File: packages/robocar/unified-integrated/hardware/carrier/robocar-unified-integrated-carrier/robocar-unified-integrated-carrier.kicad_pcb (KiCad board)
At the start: 2 copper layers, 94 x 100 mm, 108 parts, among them J1 IDC 2x7 head cable, J11 Test: 3V3 5V GND VBAT, J12 Test: GND SDA SCL RST, J13 GND post, J14 GND post, J15 UART0 TX tap, J16 IDC 2x7 head cable, J17 IDC 2x7 head cable, J18 GPIO A/B, J19 Speaker, J2 IDC 2x7 head cable, J20 Pan servo (SG90), J21 Tilt servo (SG90), J22 Left RGB LED, J23 Right RGB LED, J3 XT30 pack in, J5 Motor left, J6 Motor right, J7 RCWL-1601 front, J8 RCWL-1601 rear, J9 SSD1306 0.91in, U1 XIAO ESP32-S3 Sense, U10 TPS563208, U2 AMS1117-3.3, U3 XIAO ESP32-S3 Sense, U4 XIAO ESP32-S3 Sense, U5 TCA9548APWR, U6 PCA9685PW, U7 TB6612FNG, U8 MAX98357AETE+, U9 MCP23017-E/SS

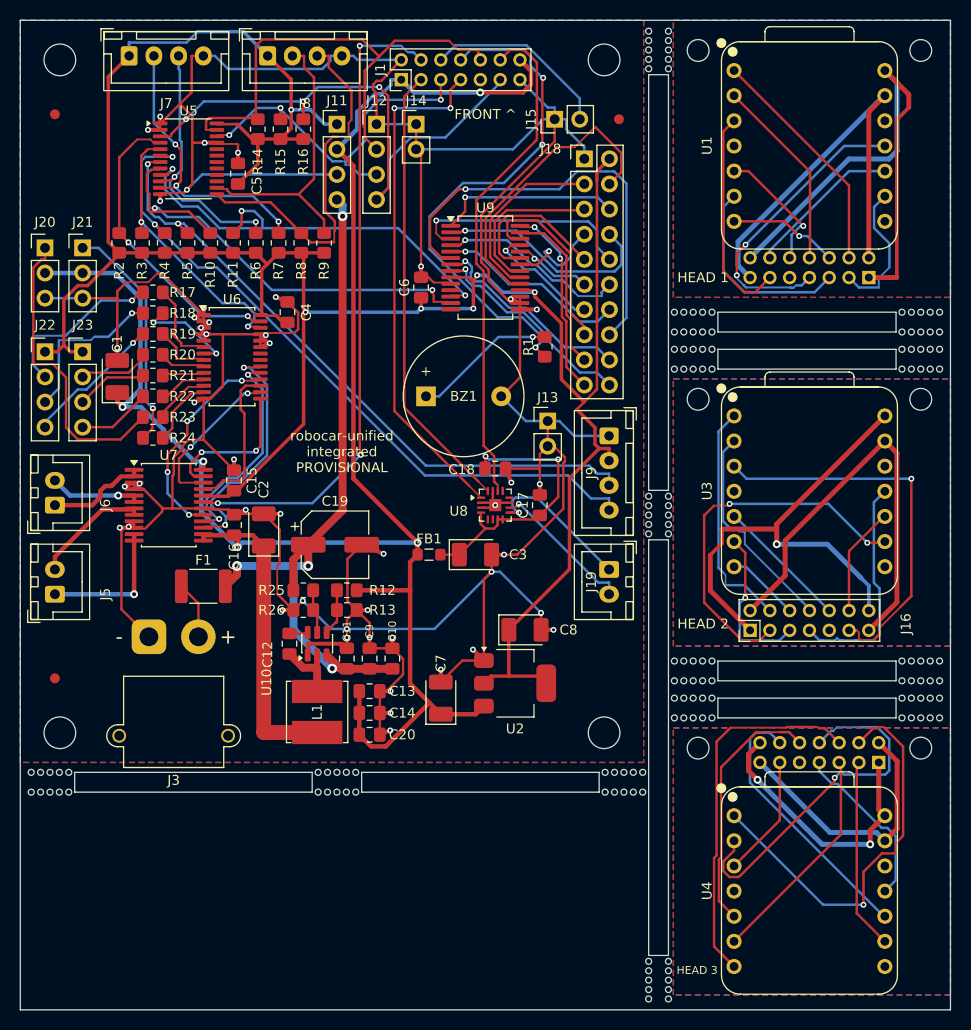
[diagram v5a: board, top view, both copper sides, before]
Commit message: fix(robocar-unified-integrated): fix the power paths the layout review found (#818)
* feat(kicad): [fanout] own pads take a via of their own

A pad joined by a fixed track to another pad that has a via counted as
having one, so the integrated carrier's buck GND pin (U10:1), tied under
the package to C11, never got a via beside it. An `own` pad ignores that
chain and takes its own via (TI's first layout rule for the TPS563208).

Co-Authored-By: Claude Opus 5.5 <noreply@anthropic.com>
Claude-Session: https://claude.ai/code/session_01DgeoMcrSCUfJwedu77q6oo

* fix(robocar-unified-integrated): fix the power paths the layout review found

The pre-fab layout review of the integrated carrier found the buck's output
capacitors 75 mm of track from L1 and the pack input on a 0.25 mm track,
neither visible to a gate. Fixed tracks in board.toml now:

- chain C13, C14 and C20 onto L1's output pad, and run the trunk and a 1 mm
  east branch (C7, the LDO, FB1) from that node;
- give the feedback divider its own sense track from C20;
- carry PACK_IN on 2 mm from the XT30 to F1;
- run C12 straight into L1 so U10's GND pin gets its own via.

C5, C6 and C18 move beside the pins they decouple, C21 adds 10 uF at the
TB6612FNG's VM1, the GND pour stops 1 mm short of the mouse-bite slot, and
R26 becomes 36 k so EN is guaranteed on by 6.3 V rather than 7.2 V. The
README records each finding with before and after measurements, and that
the pack takes an external 2S BMS.

Routed with KiCad 10.0.7 (the stamp records it), not the pinned 10.0.6.

Co-Authored-By: Claude Opus 5.5 <noreply@anthropic.com>
Claude-Session: https://claude.ai/code/session_01DgeoMcrSCUfJwedu77q6oo

* docs(robocar-unified-integrated): correct the layout fixes table

The M1 row said VM1 and the servos reach L1 with no via. They still share
one 0.8/0.4 mm via: the measuring script joined B.Cu track ends to F.Cu
tracks they only cross. The m1, m2 and m5 rows take the second review's
layer-aware measurements, and its findings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
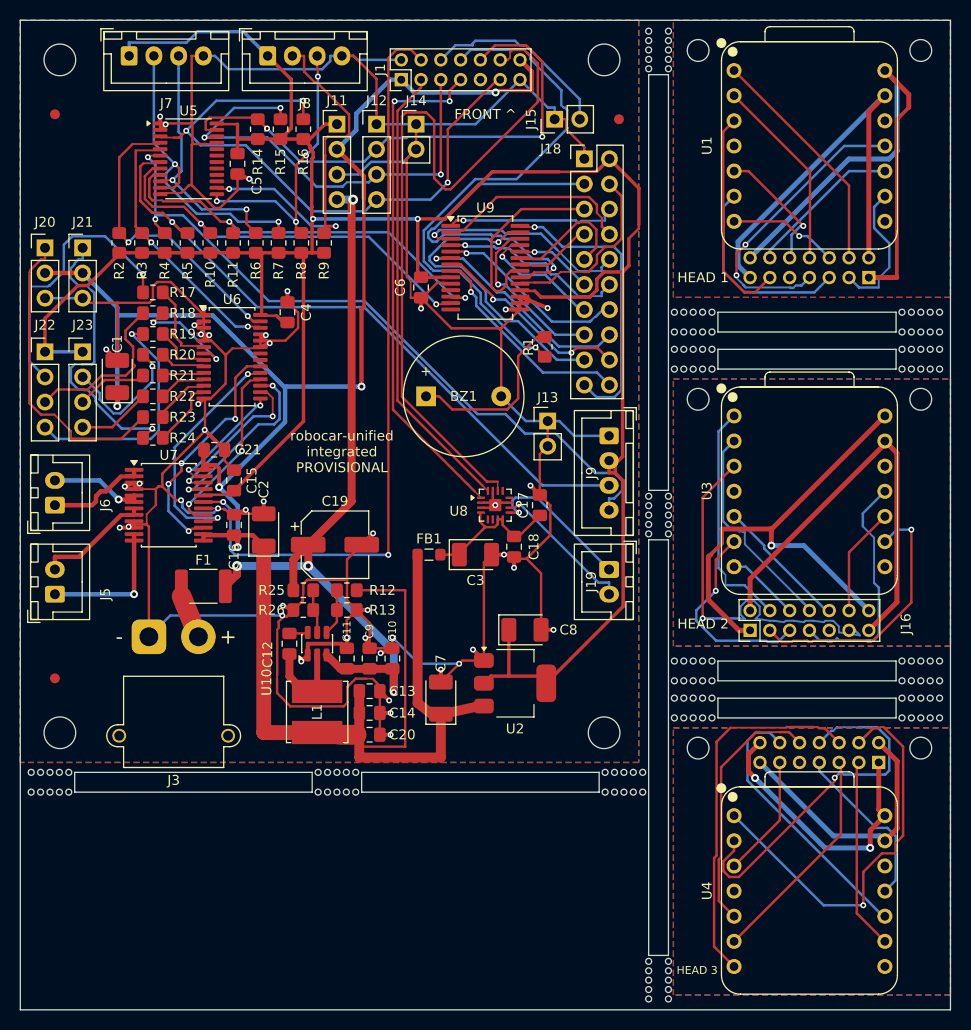
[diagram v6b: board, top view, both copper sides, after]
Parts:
- added C21: 10uF 25V, Capacitor_SMD:C_0805_2012Metric_Pad1.18x1.45mm_HandSolder, F.Cu at (119.6, 143.4)
- R26: value 30k -> 36k
- moved C18 8.13 mm to (149.9, 153.2), turned to -90 degrees
- moved C5 1.00 mm to (122.0, 114.5), turned to -90 degrees
- turned C6 to -90 degrees
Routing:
- net I2S_LRCLK: track 51.4 -> 75.7 mm
- net EXP_GPB5: track 43.7 -> 23.1 mm
- net EXP_INTA: track 18.6 -> 36.8 mm, vias 0 -> 1
- net EXP_GPA6: track 16.9 -> 31.2 mm, vias 0 -> 1
- net AMP_5V: track 29.0 -> 15.6 mm, vias 2 -> 0
- net GND: track 441.0 -> 428.4 mm, vias 46 -> 44
- net +5V: track 207.7 -> 220.2 mm
- net EXP_INTB: track 30.8 -> 18.7 mm
- net MOTOR_STBY: track 66.1 -> 77.6 mm, vias 3 -> 2
- net LED_L_R: track 17.6 -> 28.3 mm
- net HEAD2_I2S_BCLK: track 37.9 -> 27.3 mm, vias 2 -> 1
- net LED_L_B: track 14.1 -> 24.4 mm
- net EXP_GPA7: track 19.6 -> 29.7 mm, vias 2 -> 1
- net I2C_SCL: track 37.5 -> 47.4 mm
- net CH4_SDA: track 37.5 -> 28.6 mm, vias 0 -> 4
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
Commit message: fix(robocar-unified-integrated): fix the second layout review's findings
- VBAT into the buck on 1.0/0.5 mm vias only; the sense track and the FB1
  branch move east and C10 0.3 mm east to make room, and B.Cu route keepouts
  hold VBAT off the feedback divider and a stray GND run off its via.
- +5V takes its own net class with 1.0/0.5 mm vias.
- C15 turned so its GND pad faces U7's GND pin (20.6 mm to 5.4 mm), and its
  GND pad now needs a fanout via.
- Head pours start 1 mm short of the mouse-bite slot: 0.70 mm to every hole.
- R12 54.9 k to 56 k: 5.07 V, at or above the TB6612FNG's VM >= 5 V row.
- C11 and C10 swap, so the 10 uF sits beside VIN.

The README's before/after table is re-measured with layer-aware scripts.

Co-Authored-By: Claude Opus 5.5 <noreply@anthropic.com>
Claude-Session: https://claude.ai/code/session_01DgeoMcrSCUfJwedu77q6oo
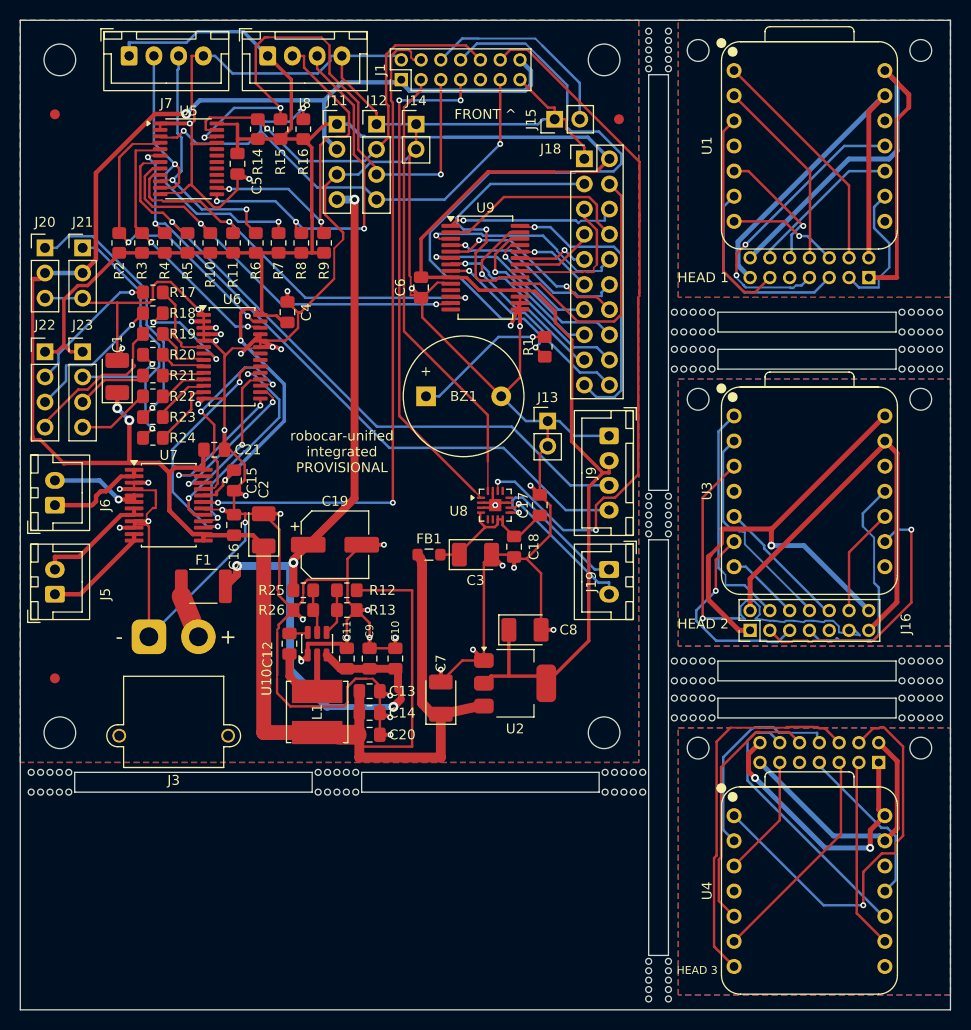
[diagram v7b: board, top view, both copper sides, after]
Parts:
- C10: value 10uF 25V -> 100nF
- C11: value 100nF -> 10uF 25V
- R12: value 54.9k -> 56k
- moved C10 0.30 mm to (137.9, 164.5)
- turned C15 to -90 degrees
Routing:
- net GND: track 428.4 -> 457.2 mm, vias 44 -> 42
- net HEAD3_PIEZO: track 36.7 -> 21.0 mm, vias 1 -> 0
- net LED_L_R: track 28.3 -> 14.0 mm
- net I2C_SDA: track 54.2 -> 42.4 mm, vias 2 -> 1
- net PIEZO: track 55.4 -> 67.0 mm
- net EXP_GPA6: track 31.2 -> 20.3 mm
- net I2C_SCL: track 47.4 -> 57.9 mm
- net MOTOR_STBY: track 77.6 -> 68.4 mm
- net CH4_SDA: track 28.6 -> 37.5 mm, vias 4 -> 3
- net LED_L_B: track 24.4 -> 15.6 mm, vias 1 -> 0
- net EXP_INTA: track 36.8 -> 28.1 mm
- net MUX_RST: track 61.7 -> 54.2 mm
- net EXP_INTB: track 18.7 -> 25.8 mm
- net EXP_GPA2: track 13.1 -> 7.26 mm, vias 0 -> 1
- net EXP_GPA0: track 20.0 -> 14.5 mm
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
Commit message: fix(robocar-unified-integrated): widen 5V to 0.8 mm and tie U7's signal GND
The fourth layout review found the servo feed necked to 0.337 mm along the
left edge, with the head cable's 5V running through the same neck. +5V's
class goes from 0.45 to 0.8 mm: Freerouting necks the last millimetre into
the TB6612FNG's pins (0.40 mm) and routes the rest wide. The servos and the
head cable now take separate paths, each through its own 1.0/0.5 mm via;
estimated DC resistance from L1 to the head cable falls from 124 to 45 mOhm.

U7:18, which lost its pour contact when C15 turned, gets a fixed 0.3 mm
track to C16's GND pad and via. The README table is re-measured.

Co-Authored-By: Claude Opus 5.5 <noreply@anthropic.com>
Claude-Session: https://claude.ai/code/session_01DgeoMcrSCUfJwedu77q6oo
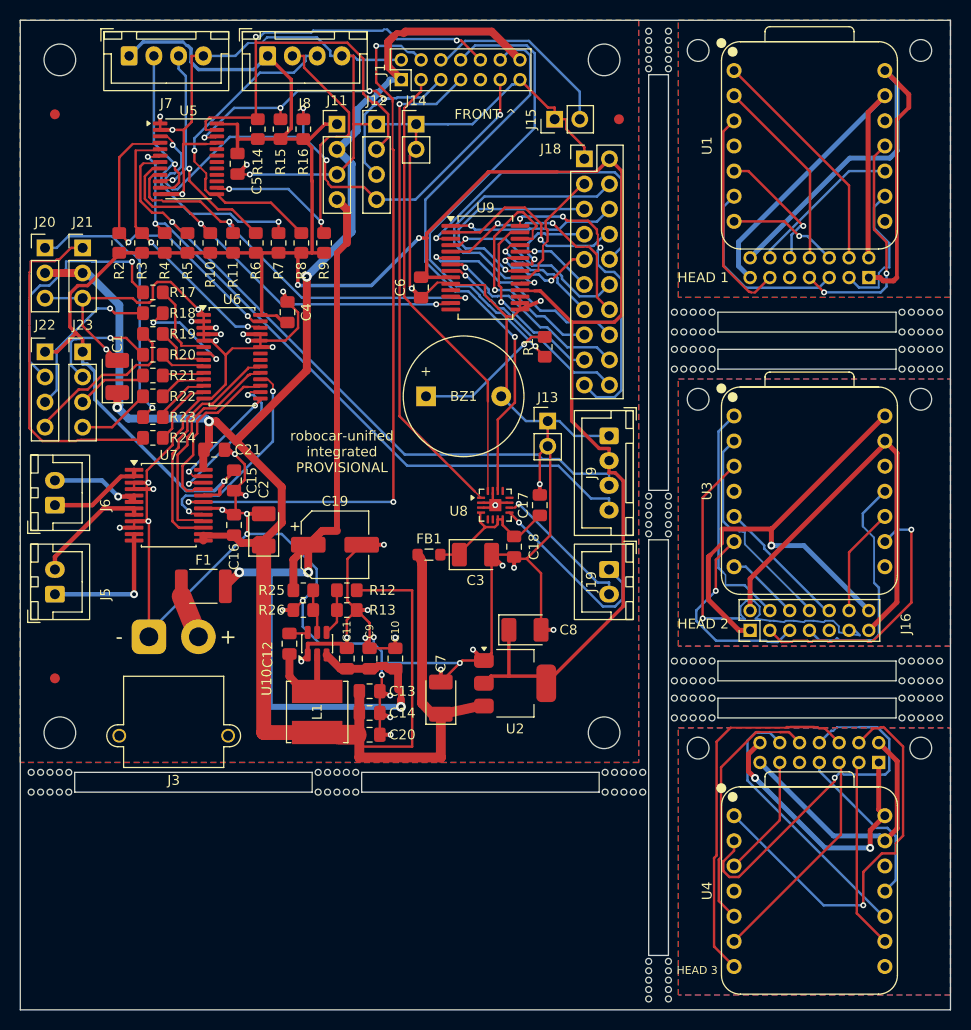
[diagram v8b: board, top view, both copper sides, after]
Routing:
- net GND: track 457.2 -> 435.4 mm, vias 42 -> 47
- net I2C_SDA: track 42.4 -> 62.6 mm, vias 1 -> 2
- net I2C_SCL: track 57.9 -> 39.3 mm, vias 3 -> 4
- net PIEZO: track 67.0 -> 49.5 mm
- net HEAD3_PIEZO: track 21.0 -> 36.7 mm, vias 0 -> 1
- net EXP_INTA: track 28.1 -> 13.1 mm, vias 1 -> 0
- net I2S_LRCLK: track 71.8 -> 57.4 mm, vias 2 -> 1
- net LED_L_R: track 14.0 -> 24.7 mm
- net SERVO_TILT: track 24.5 -> 34.9 mm, vias 1 -> 0
- net EXP_GPB2: track 21.5 -> 31.9 mm
- net +5V: track 219.8 -> 211.4 mm
- net EXP_GPA5: track 16.6 -> 25.0 mm
- net EXP_GPA0: track 14.5 -> 22.2 mm, vias 0 -> 1
- net VBAT: track 86.6 -> 93.6 mm, vias 4 -> 3
- net HEAD_I2S_DIN: track 30.3 -> 23.8 mm
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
